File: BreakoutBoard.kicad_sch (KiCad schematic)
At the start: 24 parts, among them J1 PJ-063AH, J10 10129381-906001BLF, J2 10129381-906001BLF, J3 10129381-906001BLF, J4 10129381-906001BLF, J5 RJHSE-5384, J6 10129381-906001BLF, J9 10129381-920001BLF, U1 AL5809-20S1-7

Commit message: updated RJ45 connector part number and fixed silk screen mistakes on GPIO numbering
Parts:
- J5: MOUSER# 523-RJHSE-5384 -> 523-RJHSE-5381
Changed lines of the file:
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@@
 			)
 		)
-		(property "MOUSER#" "523-RJHSE-5384"
+		(property "MOUSER#" "523-RJHSE-5381"
 			(at 173.99 107.95 0)
 			(effects

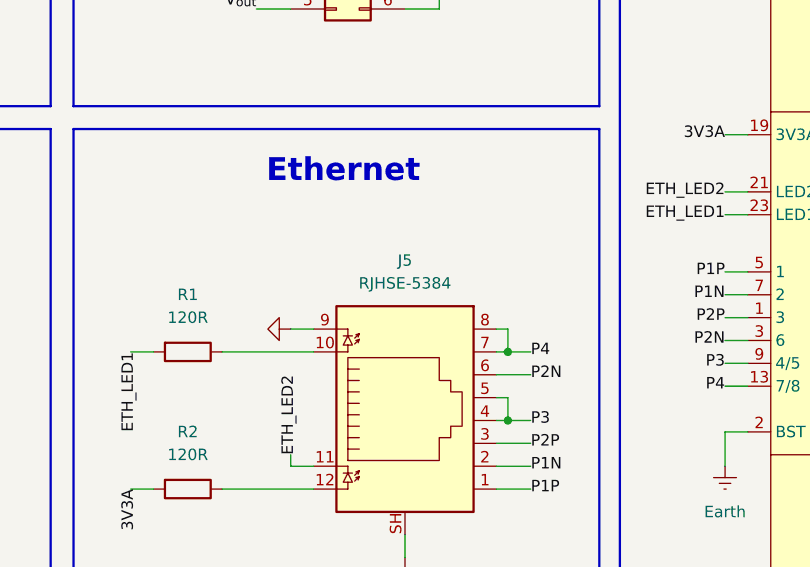
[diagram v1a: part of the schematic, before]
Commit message: fixed RJ45 connector type value
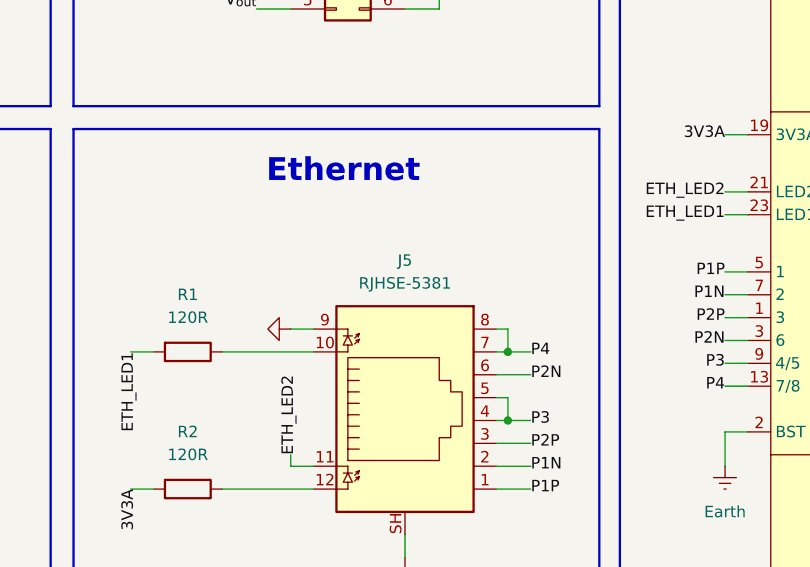
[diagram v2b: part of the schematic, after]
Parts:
- J5: value RJHSE-5384 -> RJHSE-5381
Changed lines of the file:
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@@
 			)
 		)
-		(property "Value" "RJHSE-5384"
+		(property "Value" "RJHSE-5381"
 			(at 173.99 92.71 0)
 			(effects

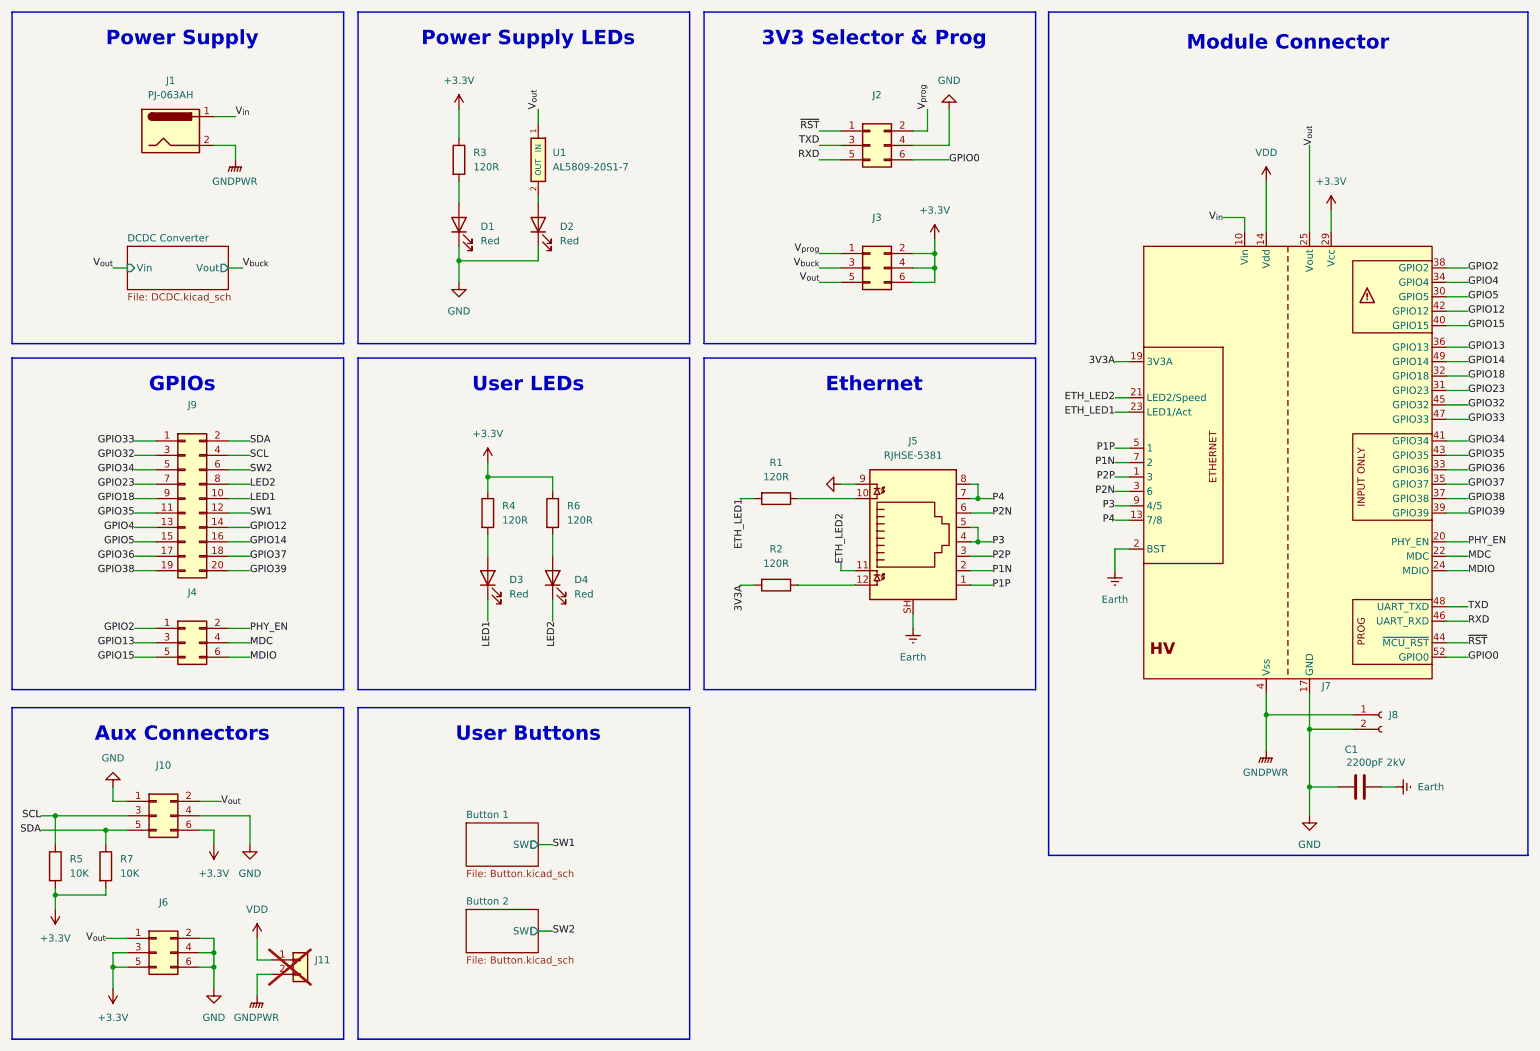
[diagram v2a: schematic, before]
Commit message: completed routing for revision 0.2
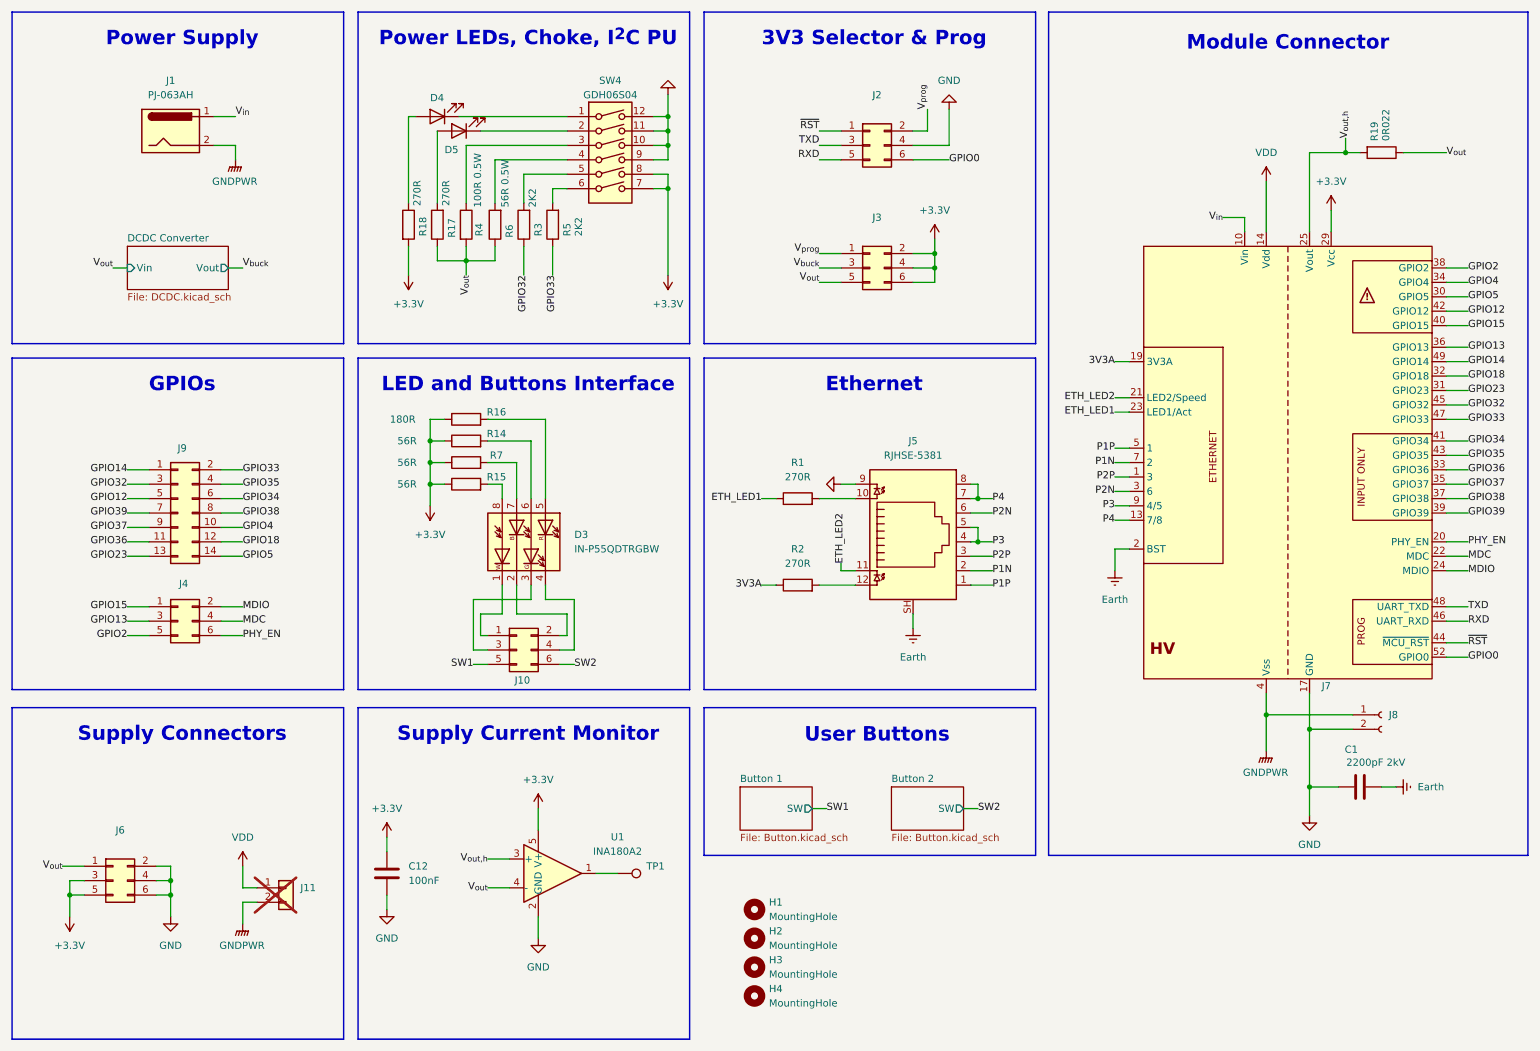
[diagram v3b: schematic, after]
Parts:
- removed D1, D2, D3: Red, LED_SMD:LED_0603_1608Metric, symbol Device:LED
- removed J9: 10129381-920001BLF, Connector_PinHeader_2.54mm:PinHeader_2x10_P2.54mm_Vertical, symbol Connector_Generic:Conn_02x10_Odd_Even
- removed U1: AL5809-20S1-7, Project:SODFL3717X100N, symbol Project:AL5809
- added C12: 100nF, Capacitor_SMD:C_0805_2012Metric, symbol Device:C
- added D3: IN-P55QDTRGBW, Project:INP55QDTRGBW, symbol Project:Inolux_P55QDTRGBW
- added D5: Red, LED_SMD:LED_0603_1608Metric, symbol Device:LED
- added H1, H2, H3, H4: MountingHole, MountingHole:MountingHole_3.2mm_M3, symbol Mechanical:MountingHole
- added J9: 10129381-914001BLF, Connector_PinHeader_2.54mm:PinHeader_2x07_P2.54mm_Vertical, symbol Connector_Generic:Conn_02x07_Odd_Even
- added R14, R15: 56R, Resistor_SMD:R_0805_2012Metric, symbol Device:R
- added R16: 180R, Resistor_SMD:R_0805_2012Metric, symbol Device:R
- added R17, R18: 270R, Resistor_SMD:R_0805_2012Metric, symbol Device:R
- added R19: 0R022, Resistor_SMD:R_0805_2012Metric, symbol Device:R
- added SW4: GDH06S04, Project:GDH06S04, symbol Switch:SW_DIP_x06
- added TP1: TestPoint, TestPoint:TestPoint_Pad_D3.0mm, symbol Connector:TestPoint
- added U1: INA180A2, Package_TO_SOT_SMD:SOT-23-5, symbol Amplifier_Current:INA180A2
- R1, R2: value 120R -> 270R; footprint Resistor_SMD:R_0402_1005Metric -> Resistor_SMD:R_0805_2012Metric; MOUSER# 652-CR0402FX-1200GLF -> 791-WR08X2700FTL
- R3: value 120R -> 2K2; footprint Resistor_SMD:R_0402_1005Metric -> Resistor_SMD:R_0805_2012Metric; MOUSER# 652-CR0402FX-1200GLF -> 791-WR08X222JTL
- R4: value 120R -> 100R 0.5W; footprint Resistor_SMD:R_0402_1005Metric -> Resistor_SMD:R_0805_2012Metric; MOUSER# 652-CR0402FX-1200GLF -> 71-CRCW0805100RFKEAH
- R5: value 10K -> 2K2; footprint Resistor_SMD:R_0402_1005Metric -> Resistor_SMD:R_0805_2012Metric; MOUSER# 603-RE0402FRE0710KL -> 791-WR08X222JTL
- R6: value 120R -> 56R 0.5W; footprint Resistor_SMD:R_0402_1005Metric -> Resistor_SMD:R_0805_2012Metric; MOUSER# 652-CR0402FX-1200GLF -> 660-SG73S2ATTD56R0F
- R7: value 10K -> 56R; footprint Resistor_SMD:R_0402_1005Metric -> Resistor_SMD:R_0805_2012Metric; MOUSER# 603-RE0402FRE0710KL -> 603-AC0805FR-0756RL
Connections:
- net +3.3V: now also R7.1, C12.2, R14.1, R15.1, R16.1, R18.2, SW4.7, SW4.8, U1.5 (V+); no longer J10.6 (Pin_6), R3.1, R4.1, R5.2, R6.1, R7.2
- net 3V3A: now also R2.1; no longer R2.2
- net ETH_LED1: now also R1.1; no longer R1.2
- net GND: now also C12.1, SW4.10, SW4.11, SW4.12, SW4.9, U1.2 (GND); no longer J10.1 (Pin_1), J10.4 (Pin_4)
- net GPIO12: now also J9.5 (Pin_5)
- net GPIO14: now also J9.1 (Pin_1)
- net GPIO15: now also J4.1 (Pin_1); no longer J4.5 (Pin_5)
- net GPIO18: now also J9.12 (Pin_12)
- net GPIO2: now also J4.5 (Pin_5); no longer J4.1 (Pin_1)
- net GPIO23: now also J9.13 (Pin_13)
- net GPIO32: now also R3.1, J9.3 (Pin_3)
- net GPIO33: now also R5.1, J9.2 (Pin_2)
- net GPIO34: now also J9.6 (Pin_6)
- net GPIO35: now also J9.4 (Pin_4)
- net GPIO36: now also J9.11 (Pin_11)
- net GPIO37: now also J9.9 (Pin_9)
- net GPIO38: now also J9.8 (Pin_8)
- net GPIO39: now also J9.7 (Pin_7)
- net GPIO4: now also J9.10 (Pin_10)
- net GPIO5: now also J9.14 (Pin_14)
- net MDIO: now also J4.2 (Pin_2); no longer J4.6 (Pin_6)
- net PHY_EN: now also J4.6 (Pin_6); no longer J4.2 (Pin_2)
- net SW1: now also J10.5 (Pin_5)
- net SW2: now also J10.6 (Pin_6)
- net V_{out}: now also R4.2, R6.1, R17.1, R19.1, U1.4 (-); no longer J10.2 (Pin_2), J7.25 (Vout), J7.26 (Vout), J7.27 (Vout), J7.28 (Vout)
- net at J5.12: now also R2.2; no longer R2.1
- net at D4.2 (A): now also R18.1; no longer R6.2
- net at J5.10: now also R1.2; no longer R1.1
- net at R3.2: now also SW4.5
- net LED2: no longer names the net of D4.1 (K)
- net LED2: now also SW4.1
- net SCL: no longer names the net of J10.3 (Pin_3)
- net SCL: now also D3.3 (KG); no longer R5.1
- removed net SDA: J10.5 (Pin_5), R7.1
- new net: D3.7 (AB), R7.2
- new net: D3.6 (AG), R14.2
- new net: D3.5 (AR), R16.2
- new net: R5.2, SW4.6
- new net: R6.2, SW4.4
- new net: D5.1 (K), SW4.2
- new net: R4.1, SW4.3
- new net: D5.2 (A), R17.2
- new net: TP1.1, U1.1
- new net: D3.1 (KW), J10.1 (Pin_1)
- new net: D3.2 (KB), J10.2 (Pin_2)
- new net: D3.4 (KR), J10.4 (Pin_4)
- new net: D3.8 (AW), R15.2
- new net V_{out,h}: J7.25 (Vout), J7.26 (Vout), J7.27 (Vout), J7.28 (Vout), R19.2, U1.3 (+)
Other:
- note added: "LED and Buttons Interface"
- note added: "Power LEDs, Choke, I^{2}C PU"
- note added: "Supply Connectors"
- note added: "Supply Current Monitor"
- note removed: "Aux Connectors"
- note removed: "Power Supply LEDs"
- note removed: "User LEDs"
- moved on the sheet: J11, J4, J6

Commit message: completed silk screen
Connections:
- net GPIO14: now also J9.2 (Pin_2); no longer J9.1 (Pin_1)
- net GPIO32: now also R5.1; no longer R3.1
- net GPIO33: now also J9.1 (Pin_1), R3.1; no longer J9.2 (Pin_2), R5.1
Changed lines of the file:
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@@
+	(wire
+		(pts
+			(xy 110.49 55.88) (xy 110.49 60.96)
+		)
+		(stroke
+			(width 0)
+			(type default)
+		)
+	)
 	(wire
 		(pts
@@
 	(wire
 		(pts
+			(xy 35.56 95.25) (xy 39.37 95.25)
+		)
+		(stroke
+			(width 0)
+			(type default)
+		)
+	)
+	(wire
+		(pts
 			(xy 99.06 93.98) (xy 104.14 93.98)
 		)
@@
 	(wire
 		(pts
-			(xy 35.56 95.25) (xy 39.37 95.25)
-		)
-		(stroke
-			(width 0)
-			(type default)
-		)
-	)
-	(wire
-		(pts
 			(xy 157.48 57.15) (xy 161.29 57.15)
 		)
@@
 	(wire
 		(pts
+			(xy 105.41 55.88) (xy 105.41 60.96)
+		)
+		(stroke
+			(width 0)
+			(type default)
+		)
+	)
+	(wire
+		(pts
 			(xy 58.42 168.91) (xy 55.88 168.91)
 		)
@@
 	(wire
 		(pts
+			(xy 52.07 95.25) (xy 55.88 95.25)
+		)
+		(stroke
+			(width 0)
+			(type default)
+		)
+	)
+	(wire
+		(pts
 			(xy 88.9 93.98) (xy 88.9 90.17)
 		)
@@
 	(wire
 		(pts
-			(xy 52.07 95.25) (xy 55.88 95.25)
-		)
-		(stroke
-			(width 0)
-			(type default)
-		)
-	)
-	(wire
-		(pts
 			(xy 209.55 82.55) (xy 212.09 82.55)
 		)
@@
 	(wire
 		(pts
-			(xy 110.49 55.88) (xy 110.49 60.96)
-		)
-		(stroke
-			(width 0)
-			(type default)
-		)
-	)
-	(wire
-		(pts
 			(xy 130.81 38.1) (xy 130.81 40.64)
 		)
@@
 		(pts
 			(xy 176.53 31.75) (xy 176.53 35.56)
-		)
-		(stroke
-			(width 0)
-			(type default)
-		)
-	)
-	(wire
-		(pts
-			(xy 105.41 55.88) (xy 105.41 60.96)
 		)
 		(stroke
@@
 	)
 	(label "GPIO32"
-		(at 105.41 60.96 270)
+		(at 110.49 60.96 270)
 		(effects
 			(font
@@
 	)
 	(label "GPIO33"
-		(at 55.88 95.25 0)
-		(effects
-			(font
-				(size 1.27 1.27)
-			)
-			(justify left)
+		(at 35.56 95.25 180)
+		(effects
+			(font
+				(size 1.27 1.27)
+			)
+			(justify right)
 		)
 	)
@@
 	)
 	(label "GPIO14"
-		(at 35.56 95.25 180)
-		(effects
-			(font
-				(size 1.27 1.27)
-			)
-			(justify right)
+		(at 55.88 95.25 0)
+		(effects
+			(font
+				(size 1.27 1.27)
+			)
+			(justify left)
 		)
 	)
@@
 	)
 	(label "GPIO33"
-		(at 110.49 60.96 270)
-		(effects
-			(font
+		(at 105.41 60.96 270)
+		(effects
+			(font

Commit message: added IDAnything
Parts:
- C1: IDAnything (none) -> cjbd17kqpcg079c1ae8a37wt8d
- C12: IDAnything (none) -> 7306hr3vk0hr983c9yxsesf49q
- D3: IDAnything (none) -> akj4era9spgvx965qfxqvmrv2q
- D4, D5: IDAnything (none) -> 9yjsdfr89jkcm9fg1nkrfp7y0f
- J1: IDAnything (none) -> 157a0me1drjvka0r0ztpant4fe
- J10, J2, J3, J4, J6: IDAnything (none) -> 74h3vv7nmakgnaj3dje14gm1cg
- J5: IDAnything (none) -> ak2rtrj5wwjn58jx1er1822wfh
- J9: IDAnything (none) -> 29xjwbg9h6jhr918v14h6n0ga0
- R1, R17, R18, R2: IDAnything (none) -> 8qy9kfpz4rjz68060b2d6hntm0
- R14, R15, R7: IDAnything (none) -> 4q4mn9485pkh08a21zezck8s11
- R16: IDAnything (none) -> chpvqwnx6tjr29bf3xacjea7ne
- R19: IDAnything (none) -> 78ybqpgsmgj0q88nxqycedz057
- R3, R5: IDAnything (none) -> ajyg8a6kw8j8kbtq4yep9zt199
- R4: IDAnything (none) -> e4khx4jva8k0wb08y4n5nr9g3p
- R6: IDAnything (none) -> 3wqsdtgvapkr89r2zkev0hyecg
- SW4: IDAnything (none) -> 2y9tnwrs5yg5t9326kw182cy70
- U1: IDAnything (none) -> 8ndc6mjn78hgtbdb7ac5ptjd0f

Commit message: arranged reference designators
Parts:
- D4, D5: IDAnything 9yjsdfr89jkcm9fg1nkrfp7y0f -> (none); MOUSER# 720-LSQ976.01-N1Q2-1 -> 720-KRELPS122VGVI23H
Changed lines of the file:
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@@
 			)
 		)
-		(property "MOUSER#" "720-LSQ976.01-N1Q2-1"
+		(property "MOUSER#" "720-KRELPS122VGVI23H"
 			(at 90.17 33.02 90)
 			(effects
@@
 			)
 		)
-		(property "IDAnything" "9yjsdfr89jkcm9fg1nkrfp7y0f"
+		(property "IDAnything" ""
 			(at 90.17 33.02 90)
 			(effects
@@
 			)
 		)
-		(property "MOUSER#" "720-LSQ976.01-N1Q2-1"
+		(property "MOUSER#" "720-KRELPS122VGVI23H"
 			(at 93.98 35.56 90)
 			(effects
@@
 			)
 		)
-		(property "IDAnything" "9yjsdfr89jkcm9fg1nkrfp7y0f"
+		(property "IDAnything" ""
 			(at 93.98 35.56 90)
 			(effects
